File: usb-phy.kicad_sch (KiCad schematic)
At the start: 105 parts, among them J12 614004184726, J13 USB4105-GF-A, J14 USB4105-GF-A, Q17 BSS138PW, U15 TPS7B8133DRVR, U16 TPD4E05U06QDQARQ1, U17 TPD4E05U06QDQARQ1, U18 SN74HC595D, U19 MAX3421EETJ+, U20 FT4232H-56Q, U21 TPD4E05U06QDQARQ1, U22 TXU0304BQAR, U23 TXU0304BQAR, U24 TXU0304BQAR, U25 TUSB1106RSVR, Y1 ABM8G-12.000MHZ-18-D2Y-T, Y2 ABM8G-12.000MHZ-18-D2Y-T

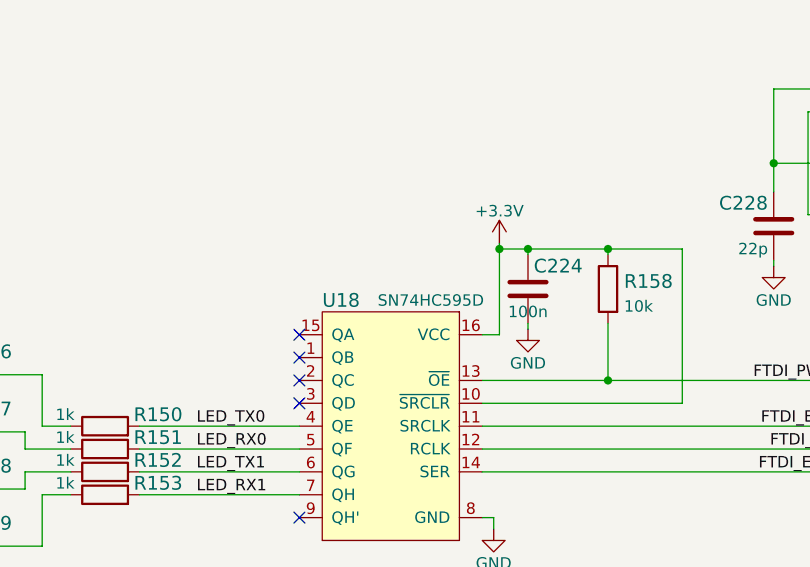
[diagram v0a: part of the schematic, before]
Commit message: Import changes to PCB. Align part of the designators
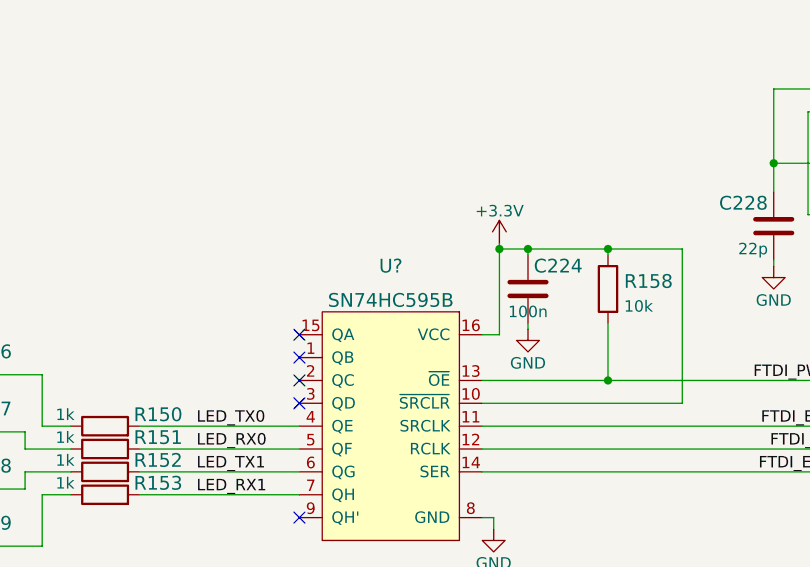
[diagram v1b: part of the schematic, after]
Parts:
- removed U18: SN74HC595D, antmicro-footprints:SOIC-16_W3.90mm, symbol antmicroLogicShiftRegisters:SN74HC595D
- added U?: SN74HC595B, antmicro-footprints:X1QFN-16-1EP_2.5x2.5mm, symbol antmicroLogicShiftRegisters:SN74HC595B
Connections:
- net +3V3: now also U?.10 (~{SRCLR}), U?.16 (VCC)
- net FTDI_EECLK: now also U?.11 (SRCLK)
- net FTDI_EECS: now also U?.12 (RCLK)
- net FTDI_EEDAT: now also U?.14 (SER)
- net FTDI_PWREN: now also U?.13 (~{OE})
- net GND: now also U?.8 (GND)
- net LED_RX0: now also U?.5 (QF)
- net LED_RX1: now also U?.7 (QH)
- net LED_TX0: now also U?.4 (QE)
- net LED_TX1: now also U?.6 (QG)
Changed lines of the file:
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@@
     (pin "1")
+  )
+  (symbol (lib_id "antmicroLogicShiftRegisters:SN74HC595B") (at 89.535 267.335 0) (mirror y) (unit 1)
+    (in_bom yes) (on_board yes) (fields_autoplaced)
+    (property "Reference" "U?" (id 0) (at 89.535 249.555 0)
+      (effects (font (size 1.524 1.524)))
+    )
+    (property "Value" "SN74HC595B" (id 1) (at 89.535 253.365 0)
+      (effects (font (size 1.524 1.524)))
+    )
+    (property "Footprint" "antmicro-footprints:X1QFN-16-1EP_2.5x2.5mm" (id 2) (at 89.535 301.625 0)
+      (effects (font (size 1.524 1.524)) (justify left) hide)
+    )
+    (property "Datasheet" "https://www.ti.com/general/docs/suppproductinfo.tsp?distId=26&gotoUrl=https://www.ti.com/lit/gpn/sn74hc595b" (id 3) (at 89.535 299.085 0)
+      (effects (font (size 1.524 1.524)) (justify left) hide)
+    )
+    (property "Manufacturer" "Texas Instruments" (id 4) (at 89.535 294.005 0)
+      (effects (font (size 1.524 1.524)) (justify left) hide)
+    )
+    (property "MPN" "SN74HC595BRWNR" (id 5) (at 89.535 296.545 0)
+      (effects (font (size 1.524 1.524)) (justify left) hide)
+    )
+    (pin "1")
+    (pin "10")
+    (pin "11")
+    (pin "12")
+    (pin "13")
+    (pin "14")
+    (pin "15")
+    (pin "16")
+    (pin "17")
+    (pin "2")
+    (pin "3")
+    (pin "4")
+    (pin "5")
+    (pin "6")
+    (pin "7")
+    (pin "8")
+    (pin "9")
   )
   (symbol (lib_id "power:GND") (at 386.08 102.235 0) (mirror y) (unit 1)
@@
     (pin "2")
   )
-  (symbol (lib_id "antmicroLogicShiftRegisters:SN74HC595D") (at 89.535 267.335 0) (mirror y) (unit 1)
-    (in_bom yes) (on_board yes)
-    (property "Reference" "U18" (id 0) (at 81.915 253.365 0)
-      (effects (font (size 1.524 1.524)) (justify right))
-    )
-    (property "Value" "SN74HC595D" (id 1) (at 93.98 253.365 0))
-    (property "Footprint" "antmicro-footprints:SOIC-16_W3.90mm" (id 2) (at 89.535 301.625 0)
-      (effects (font (size 1.524 1.524)) (justify left) hide)
-    )
-    (property "Datasheet" "http://www.ti.com/general/docs/suppproductinfo.tsp?distId=10&gotoUrl=http%3A%2F%2Fwww.ti.com%2Flit%2Fgpn%2Fsn74hc595" (id 3) (at 89.535 299.085 0)
-      (effects (font (size 1.524 1.524)) (justify left) hide)
-    )
-    (property "Manufacturer" "Texas Instruments" (id 4) (at 89.535 294.005 0)
-      (effects (font (size 1.524 1.524)) (justify left) hide)
-    )
-    (property "MPN" "SN74HC595D" (id 5) (at 89.535 296.545 0)
-      (effects (font (size 1.524 1.524)) (justify left) hide)
-    )
-    (pin "1")
-    (pin "10")
-    (pin "11")
-    (pin "12")
-    (pin "13")
-    (pin "14")
-    (pin "15")
-    (pin "16")
-    (pin "2")
-    (pin "3")
-    (pin "4")
-    (pin "5")
-    (pin "6")
-    (pin "7")
-    (pin "8")
-    (pin "9")
-  )
   (symbol (lib_id "power:GND") (at 154.305 137.16 0) (mirror y) (unit 1)

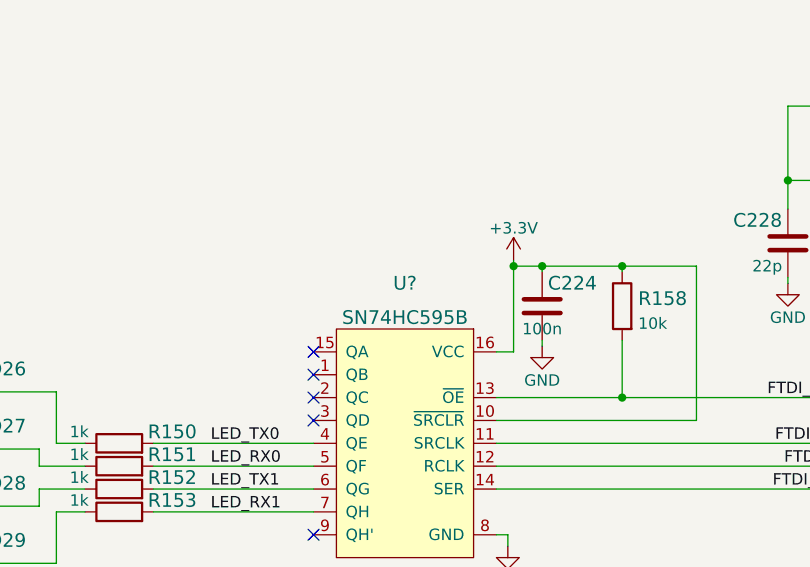
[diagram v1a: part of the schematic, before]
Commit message: Improve placement of the GBE and USB Host PHY. Update pinout for better routing
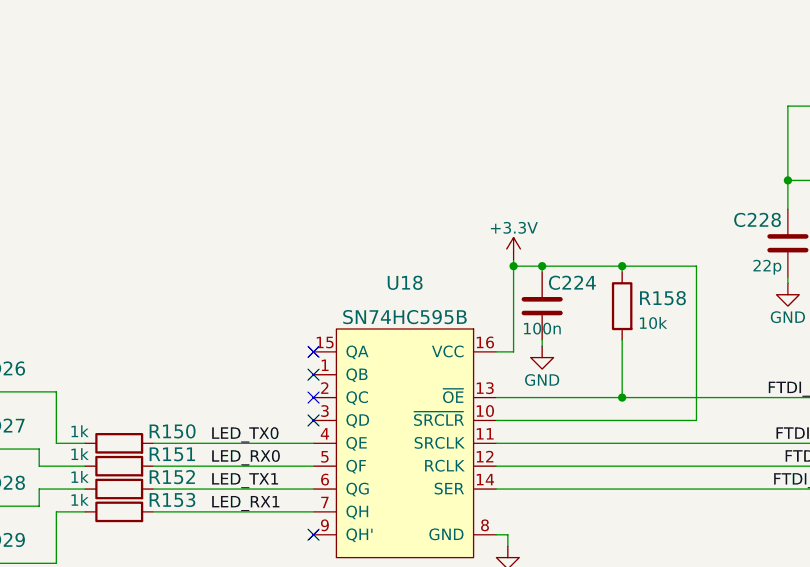
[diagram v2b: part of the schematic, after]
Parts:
- gave numbers to parts that had none: 1
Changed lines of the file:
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@@
   (symbol (lib_id "antmicroLogicShiftRegisters:SN74HC595B") (at 89.535 267.335 0) (mirror y) (unit 1)
     (in_bom yes) (on_board yes) (fields_autoplaced)
-    (property "Reference" "U?" (id 0) (at 89.535 249.555 0)
+    (property "Reference" "U18" (id 0) (at 89.535 249.555 0)
       (effects (font (size 1.524 1.524)))
     )

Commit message: Added USB power switches on USB HOST and USB USR
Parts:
- added C?: C_10u_0402, antmicro-footprints:0402-cap, symbol antmicroCapacitors0402:C_10u_0402
- added C? (x4): C_100n_0402_EIA, antmicro-footprints:0402-cap_EIA, symbol antmicroCapacitors0402:C_100n_0402_EIA
- added R? (x4): R_0R_0402, antmicro-footprints:0402-res, symbol antmicroResistors0402:R_0R_0402
- added R? (x4): R_10k_0402, antmicro-footprints:0402-res, symbol antmicroResistors0402:R_10k_0402
- added R?: R_12k4_0402, antmicro-footprints:0402-res, symbol antmicroResistors0402:R_12k4_0402
- added R?: R_2k2_0402, antmicro-footprints:0402-res, symbol antmicroResistors0402:R_2k2_0402
- added U? (x2): AP22615, antmicro-footprints:TSOT23-6, symbol antmicroPMICPowerDistributionSwitchesLoadDrivers:AP22615
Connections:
- net GND: now also C?.2, C?.2, C?.2, C?.2, C?.2, R?.1, R?.2, R?.2, R?.2, U?.2 (GND), U?.2 (GND)
- net USB_HOST_VBUS: now also C?.1, U?.1 (OUT)
- net USB_USR_VBUS: now also C?.1, C?.1, U?.1 (OUT)
- new net: R?.1, R?.1, U?.4 (EN) (x2)
- new net: R?.2, U?.3 (FLG) (x2)
- new net: R?.1, U?.5 (ISET)
- new net: R?.2, U?.5 (ISET)
- new net +5V: C?.1, C?.1, R?.1, R?.1, R?.1, R?.1, U?.6 (IN), U?.6 (IN)
- new net USB_HOST_PEN: R?.2, R?.2
- new net USB_USR_PEN: R?.2, R?.2
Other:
- note added: "TODO:"
- note added: "TODO: - add voltage label to VCCIO"
- note removed: "TODO: - add VBUS power switch"
- note removed: "TODO: - add VBUS power switch - add voltage label to VCCIO"
- moved on the sheet: C219, C220, C223, C226, C227, C231, R154, R155, R156, R157, R190, R191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

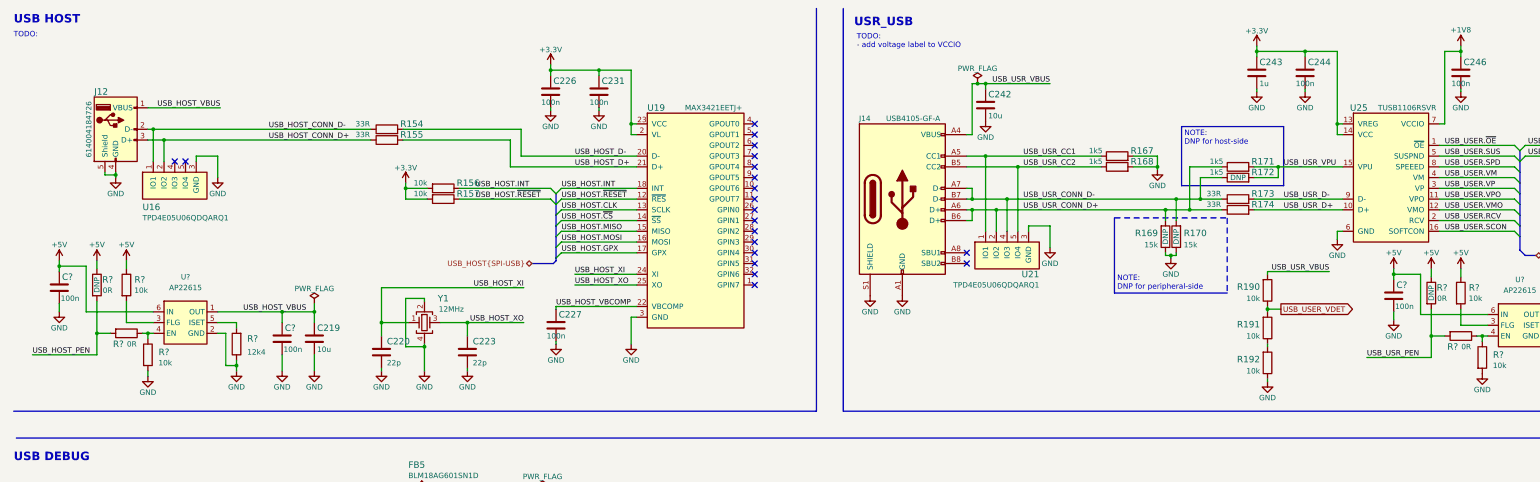
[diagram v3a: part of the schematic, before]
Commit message: Connected USB PON and DET signals to FPGA
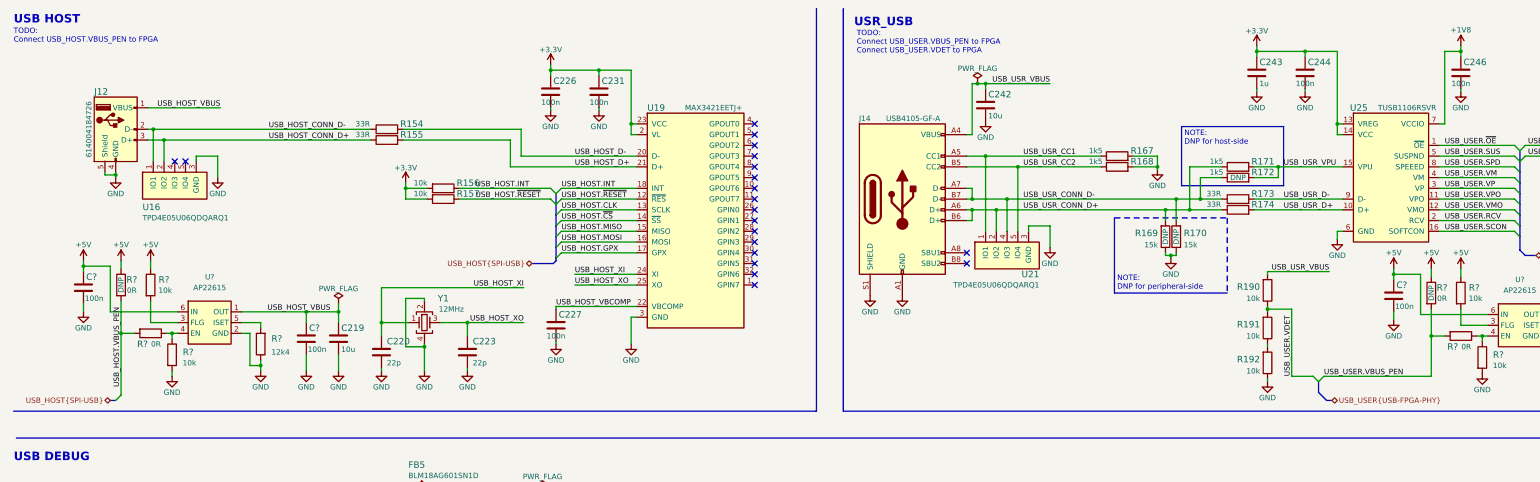
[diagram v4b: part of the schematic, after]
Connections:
- net USB_HOST_PEN renamed USB_HOST.VBUS_PEN
- net USB_USER_VDET renamed USB_USER.VDET
- net USB_USR_PEN renamed USB_USER.VBUS_PEN
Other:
- note added: "TODO: Connect USB_HOST.VBUS_PEN to FPGA"
- note added: "TODO: Connect USB_USER.VBUS_PEN to FPGA Connect USB_USER.VDET to FPGA"
- note removed: "TODO:"
- note removed: "TODO: - add voltage label to VCCIO"
- moved on the sheet: C219, C?, R?, U?

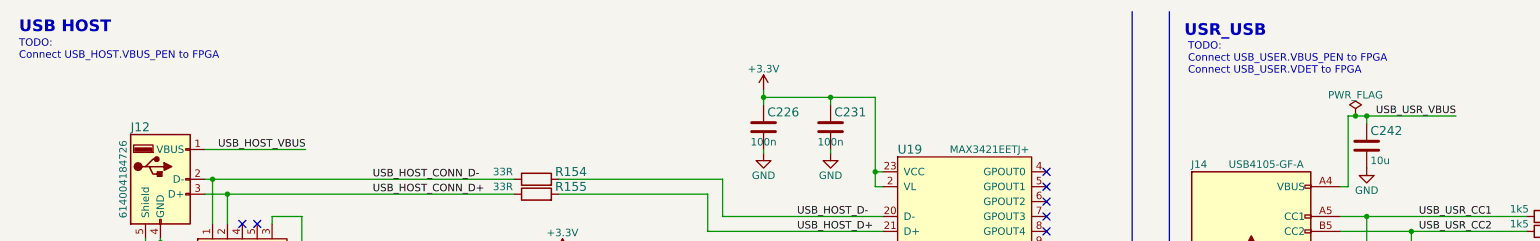
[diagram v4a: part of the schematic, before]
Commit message: Removed ToDo notes which are already done, corrected USB DET and PEN signal mapping on FPGA side, connected 200MHz generator ENA signal to FPGA
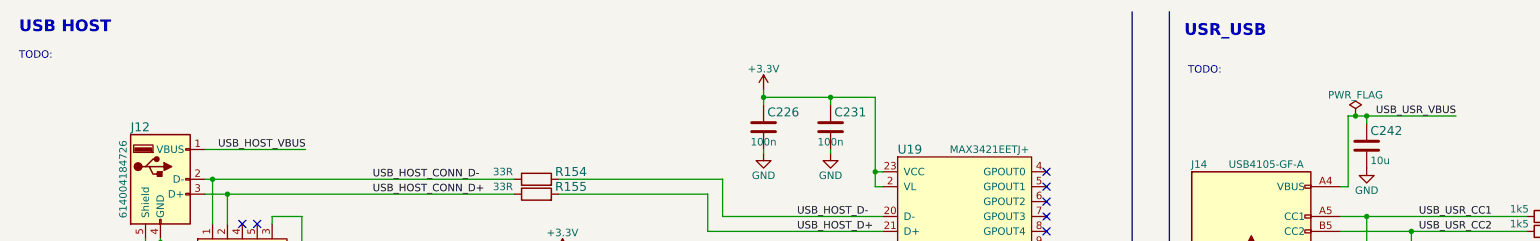
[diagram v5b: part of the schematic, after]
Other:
- note added: "TODO:"
- note removed: "TODO: Connect USB_HOST.VBUS_PEN to FPGA"
- note removed: "TODO: Connect USB_USER.VBUS_PEN to FPGA Connect USB_USER.VDET to FPGA"
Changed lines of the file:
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@@
     (effects (font (size 1.27 1.27)) (justify left bottom))
   )
-  (text "TODO:\nConnect USB_USER.VBUS_PEN to FPGA\nConnect USB_USER.VDET to FPGA"
-    (at 212.725 24.13 0)
+  (text "TODO:" (at 212.725 24.13 0)
     (effects (font (size 1.27 1.27)) (justify left bottom))
   )
@@
     (effects (font (size 1.524 1.524)) (justify left bottom))
   )
-  (text "TODO:\nConnect USB_HOST.VBUS_PEN to FPGA" (at 13.335 21.59 0)
+  (text "TODO:" (at 13.335 21.59 0)
     (effects (font (size 1.27 1.27)) (justify left bottom))
   )

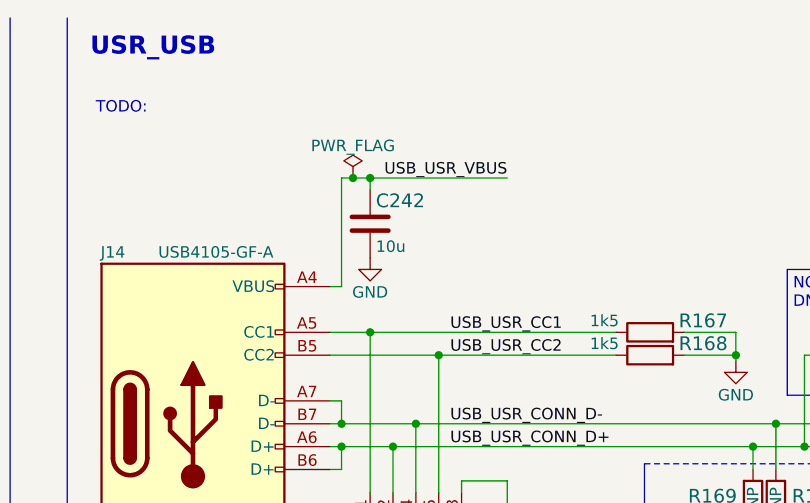
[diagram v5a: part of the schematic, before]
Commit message: Removed doubled 10uF on USR_USB VBUS
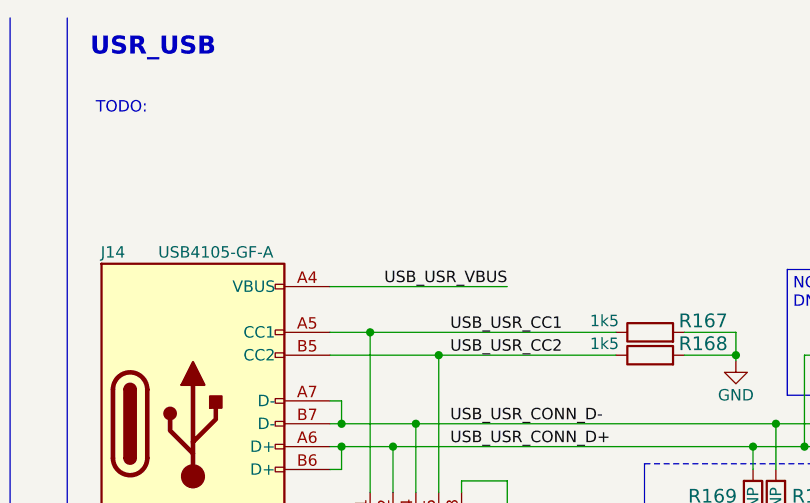
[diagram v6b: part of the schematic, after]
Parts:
- removed C242: C_10u_0402, antmicro-footprints:0402-cap, symbol antmicroCapacitors0402:C_10u_0402
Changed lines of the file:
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@@
   (junction (at 243.205 48.26) (diameter 0) (color 0 0 0 0)
   )
-  (junction (at 243.205 31.115) (diameter 0) (color 0 0 0 0)
-  )
   (junction (at 400.05 85.725) (diameter 0) (color 0 0 0 0)
   )
@@
   (junction (at 250.825 50.8) (diameter 0) (color 0 0 0 0)
   )
-  (junction (at 241.3 31.115) (diameter 0) (color 0 0 0 0)
-  )
   (junction (at 60.325 181.61) (diameter 0) (color 0 0 0 0)
   )
@@
     (stroke (width 0) (type default) (color 0 0 0 0))
   )
-  (wire (pts (xy 240.03 31.115) (xy 241.3 31.115))
+  (wire (pts (xy 238.76 43.18) (xy 258.445 43.18))
     (stroke (width 0) (type default) (color 0 0 0 0))
   )
@@
     (stroke (width 0) (type default) (color 0 0 0 0))
   )
-  (wire (pts (xy 241.3 31.115) (xy 243.205 31.115))
-    (stroke (width 0) (type default) (color 0 0 0 0))
-  )
   (wire (pts (xy 172.085 168.91) (xy 172.085 171.45))
     (stroke (width 0) (type default) (color 0 0 0 0))
@@
     (stroke (width 0) (type default) (color 0 0 0 0))
   )
-  (wire (pts (xy 240.03 31.115) (xy 240.03 43.18))
-    (stroke (width 0) (type default) (color 0 0 0 0))
-  )
   (wire (pts (xy 57.15 164.465) (xy 57.15 176.53))
     (stroke (width 0) (type default) (color 0 0 0 0))
@@
     (stroke (width 0) (type default) (color 0 0 0 0))
   )
-  (wire (pts (xy 243.205 31.115) (xy 258.445 31.115))
-    (stroke (width 0) (type default) (color 0 0 0 0))
-  )
   (wire (pts (xy 331.47 182.88) (xy 337.82 182.88))
     (stroke (width 0) (type default) (color 0 0 0 0))
@@
     (stroke (width 0) (type default) (color 0 0 0 0))
   )
-  (wire (pts (xy 243.205 31.115) (xy 243.205 32.385))
-    (stroke (width 0) (type default) (color 0 0 0 0))
-  )
   (wire (pts (xy 392.43 85.725) (xy 392.43 88.265))
     (stroke (width 0) (type default) (color 0 0 0 0))
@@
     (stroke (width 0) (type default) (color 0 0 0 0))
   )
-  (wire (pts (xy 238.76 43.18) (xy 240.03 43.18))
-    (stroke (width 0) (type default) (color 0 0 0 0))
-  )
   (wire (pts (xy 400.05 85.725) (xy 400.05 88.265))
     (stroke (width 0) (type default) (color 0 0 0 0))
@@
     (effects (font (size 1.27 1.27)) (justify left bottom))
   )
-  (label "USB_USR_VBUS" (at 258.445 31.115 180)
+  (label "USB_USR_VBUS" (at 258.445 43.18 180)
     (effects (font (size 1.27 1.27)) (justify right bottom))
   )
@@
     (pin "9")
   )
-  (symbol (lib_id "power:GND") (at 243.205 40.005 0) (unit 1)
-    (in_bom yes) (on_board yes)
-    (property "Reference" "#PWR0224" (id 0) (at 243.205 46.355 0)
-      (effects (font (size 1.524 1.524)) hide)
-    )
-    (property "Value" "GND" (id 1) (at 243.205 43.815 0))
-    (property "Footprint" "" (id 2) (at 243.205 40.005 0)
-      (effects (font (size 1.27 1.27)) hide)
-    )
-    (property "Datasheet" "" (id 3) (at 243.205 40.005 0)
-      (effects (font (size 1.27 1.27)) hide)
-    )
-    (pin "1")
-  )
   (symbol (lib_id "antmicroResistors0402:R_1k5_0402") (at 302.895 50.8 0) (unit 1)
     (in_bom yes) (on_board yes)
@@
     (pin "1")
     (pin "2")
-  )
-  (symbol (lib_id "power:PWR_FLAG") (at 241.3 31.115 0) (unit 1)
-    (in_bom yes) (on_board yes) (fields_autoplaced)
-    (property "Reference" "#FLG09" (id 0) (at 241.3 29.21 0)
-      (effects (font (size 1.524 1.524)) hide)
-    )
-    (property "Value" "PWR_FLAG" (id 1) (at 241.3 27.5392 0))
-    (property "Footprint" "" (id 2) (at 241.3 31.115 0)
-      (effects (font (size 1.27 1.27)) hide)
-    )
-    (property "Datasheet" "" (id 3) (at 241.3 31.115 0)
-      (effects (font (size 1.27 1.27)) hide)
-    )
-    (pin "1")
-  )
-  (symbol (lib_id "antmicroCapacitors0402:C_10u_0402") (at 243.205 36.195 0) (unit 1)
-    (in_bom yes) (on_board yes)
-    (property "Reference" "C242" (id 0) (at 243.84 33.655 0)
-      (effects (font (size 1.524 1.524)) (justify left))
-    )
-    (property "Value" "C_10u_0402" (id 1) (at 243.205 40.005 0)
-      (effects (font (size 1.27 1.27)) hide)
-    )
-    (property "Footprint" "antmicro-footprints:0402-cap" (id 2) (at 248.285 31.115 0)
-      (effects (font (size 1.524 1.524)) (justify left) hide)
-    )
-    (property "Datasheet" "" (id 3) (at 243.205 36.195 0)
-      (effects (font (size 1.27 1.27)) hide)
-    )
-    (property "Manufacturer" "YAGEO" (id 4) (at 248.285 26.035 0)
-      (effects (font (size 1.524 1.524)) (justify left) hide)
-    )
-    (property "MPN" "CC0402MRX5R5BB106" (id 5) (at 248.285 28.575 0)
-      (effects (font (size 1.524 1.524)) (justify left) hide)
-    )
-    (property "Val" "10u" (id 6) (at 243.84 38.735 0)
-      (effects (font (size 1.27 1.27)) (justify left))
-    )
-    (pin "1")
-    (pin "2")

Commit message: Annotated designators for new components
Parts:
- gave numbers to parts that had none: 17

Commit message: Update signage
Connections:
- net JTAG.TDO: now also R178.2; no longer R179.2
- net JTAG.TMS: now also R179.2; no longer R178.2
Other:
- moved on the sheet: C224, C228, C235, D26, D27, D28, D29, R150, R151, R152, R153, R158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
